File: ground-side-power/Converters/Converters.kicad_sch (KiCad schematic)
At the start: 31 parts, among them J10 Conn_01x03_Female, J12 Conn_01x04_Female, J13 DAQ Voltage Sensing, J14 DAQ Current Sensing, J27 Conn_01x02_Female, U3 K7805-3AR3, U4 INA180, U5 INA180, U6 URB2424LD-20WR3

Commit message: Resolved Final Issues
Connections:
- net +5V: now also J27.2 (Pin_2); no longer J27.1 (Pin_1)
- net +BATT: now also J10.2 (Pin_2); no longer J10.1 (Pin_1)
- net GND: now also J10.1 (Pin_1), J27.1 (Pin_1); no longer J10.2 (Pin_2), J27.2 (Pin_2)
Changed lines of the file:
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@@
     (effects (font (size 1.27 1.27)) (justify right))
   )
-  (hierarchical_label "+BATT" (shape input) (at 179.324 31.75 180)
+  (hierarchical_label "+BATT" (shape input) (at 179.324 34.29 180)
     (effects (font (size 1.27 1.27)) (justify right))
   )
-  (hierarchical_label "GND" (shape input) (at 179.197 54.991 180)
+  (hierarchical_label "GND" (shape input) (at 179.07 52.324 180)
     (effects (font (size 1.27 1.27)) (justify right))
   )
@@
     (effects (font (size 1.27 1.27)) (justify left))
   )
-  (hierarchical_label "+5V" (shape input) (at 179.197 52.451 180)
+  (hierarchical_label "+5V" (shape input) (at 179.07 54.864 180)
     (effects (font (size 1.27 1.27)) (justify right))
   )
@@
     (effects (font (size 1.27 1.27)) (justify right))
   )
-  (hierarchical_label "GND" (shape input) (at 179.324 34.29 180)
+  (hierarchical_label "GND" (shape input) (at 179.324 31.75 180)
     (effects (font (size 1.27 1.27)) (justify right))
   )
@@
     (pin "2")
   )
-  (symbol (lib_id "Connector:Conn_01x02_Female") (at 184.277 52.451 0) (unit 1)
-    (in_bom yes) (on_board yes) (fields_autoplaced)
-    (property "Reference" "J27" (id 0) (at 186.182 52.4509 0)
-      (effects (font (size 1.27 1.27)) (justify left))
-    )
-    (property "Value" "Conn_01x02_Female" (id 1) (at 186.182 54.9909 0)
-      (effects (font (size 1.27 1.27)) (justify left))
-    )
-    (property "Footprint" "GSP:1935310" (id 2) (at 184.277 52.451 0)
-      (effects (font (size 1.27 1.27)) hide)
-    )
-    (property "Datasheet" "~" (id 3) (at 184.277 52.451 0)
+  (symbol (lib_id "Connector:Conn_01x02_Female") (at 184.15 52.324 0) (unit 1)
+    (in_bom yes) (on_board yes) (fields_autoplaced)
+    (property "Reference" "J27" (id 0) (at 186.055 52.3239 0)
+      (effects (font (size 1.27 1.27)) (justify left))
+    )
+    (property "Value" "Conn_01x02_Female" (id 1) (at 186.055 54.8639 0)
+      (effects (font (size 1.27 1.27)) (justify left))
+    )
+    (property "Footprint" "GSP:1935310" (id 2) (at 184.15 52.324 0)
+      (effects (font (size 1.27 1.27)) hide)
+    )
+    (property "Datasheet" "~" (id 3) (at 184.15 52.324 0)
       (effects (font (size 1.27 1.27)) hide)
     )
@@
     )
     (path "/ed29890c-0b77-44d2-9f50-cf8ab77ebebf"
-      (reference "C10") (unit 1) (value "22uF") (footprint "Capacitor_SMD:C_0603_1608Metric_Pad1.08x0.95mm_HandSolder")
+      (reference "C10") (unit 1) (value "22uF") (footprint "Capacitor_SMD:C_0805_2012Metric_Pad1.18x1.45mm_HandSolder")
     )
     (path "/f316a14f-f1b7-4328-a910-be46f7f6ffff"
-      (reference "C11") (unit 1) (value "10uF") (footprint "Capacitor_SMD:C_0603_1608Metric_Pad1.08x0.95mm_HandSolder")
+      (reference "C11") (unit 1) (value "10uF") (footprint "Capacitor_SMD:C_0805_2012Metric_Pad1.18x1.45mm_HandSolder")
     )
     (path "/83e828f1-ea2c-4f92-a465-0be77eac1d2c"
-      (reference "C12") (unit 1) (value "10uF") (footprint "Capacitor_SMD:C_0603_1608Metric_Pad1.08x0.95mm_HandSolder")
+      (reference "C12") (unit 1) (value "10uF") (footprint "Capacitor_SMD:C_0805_2012Metric_Pad1.18x1.45mm_HandSolder")
     )
     (path "/578141ae-1aaf-4f14-b558-280a5eaf5853"
@@
     )
     (path "/9d81fb28-1d45-4a2d-a977-2809dd759a70"
-      (reference "C16") (unit 1) (value "10uF") (footprint "Capacitor_SMD:C_0603_1608Metric_Pad1.08x0.95mm_HandSolder")
+      (reference "C16") (unit 1) (value "10uF") (footprint "Capacitor_SMD:C_0805_2012Metric_Pad1.18x1.45mm_HandSolder")
     )
     (path "/6f03478f-34bb-4da3-ad2a-991c9dd3d62e"
@@
     )
     (path "/ec4fb15f-bcf3-43b3-a0ad-950a7d37eeb2"
-      (reference "R7") (unit 1) (value "0.01") (footprint "Resistor_SMD:R_1206_3216Metric_Pad1.30x1.75mm_HandSolder")
+      (reference "R7") (unit 1) (value "0.01") (footprint "Resistor_SMD:R_2512_6332Metric_Pad1.40x3.35mm_HandSolder")
     )
     (path "/e8b451aa-1d20-4320-9206-3705bb383e9f"
@@
     )
     (path "/1ccb64be-3251-49e5-9086-335694a2674c"
-      (reference "R9") (unit 1) (value "0.04") (footprint "Resistor_SMD:R_1206_3216Metric_Pad1.30x1.75mm_HandSolder")
+      (reference "R9") (unit 1) (value "0.04") (footprint "Resistor_SMD:R_2512_6332Metric_Pad1.40x3.35mm_HandSolder")
     )
     (path "/bb5b8186-e312-4770-869b-17d2c304a143"

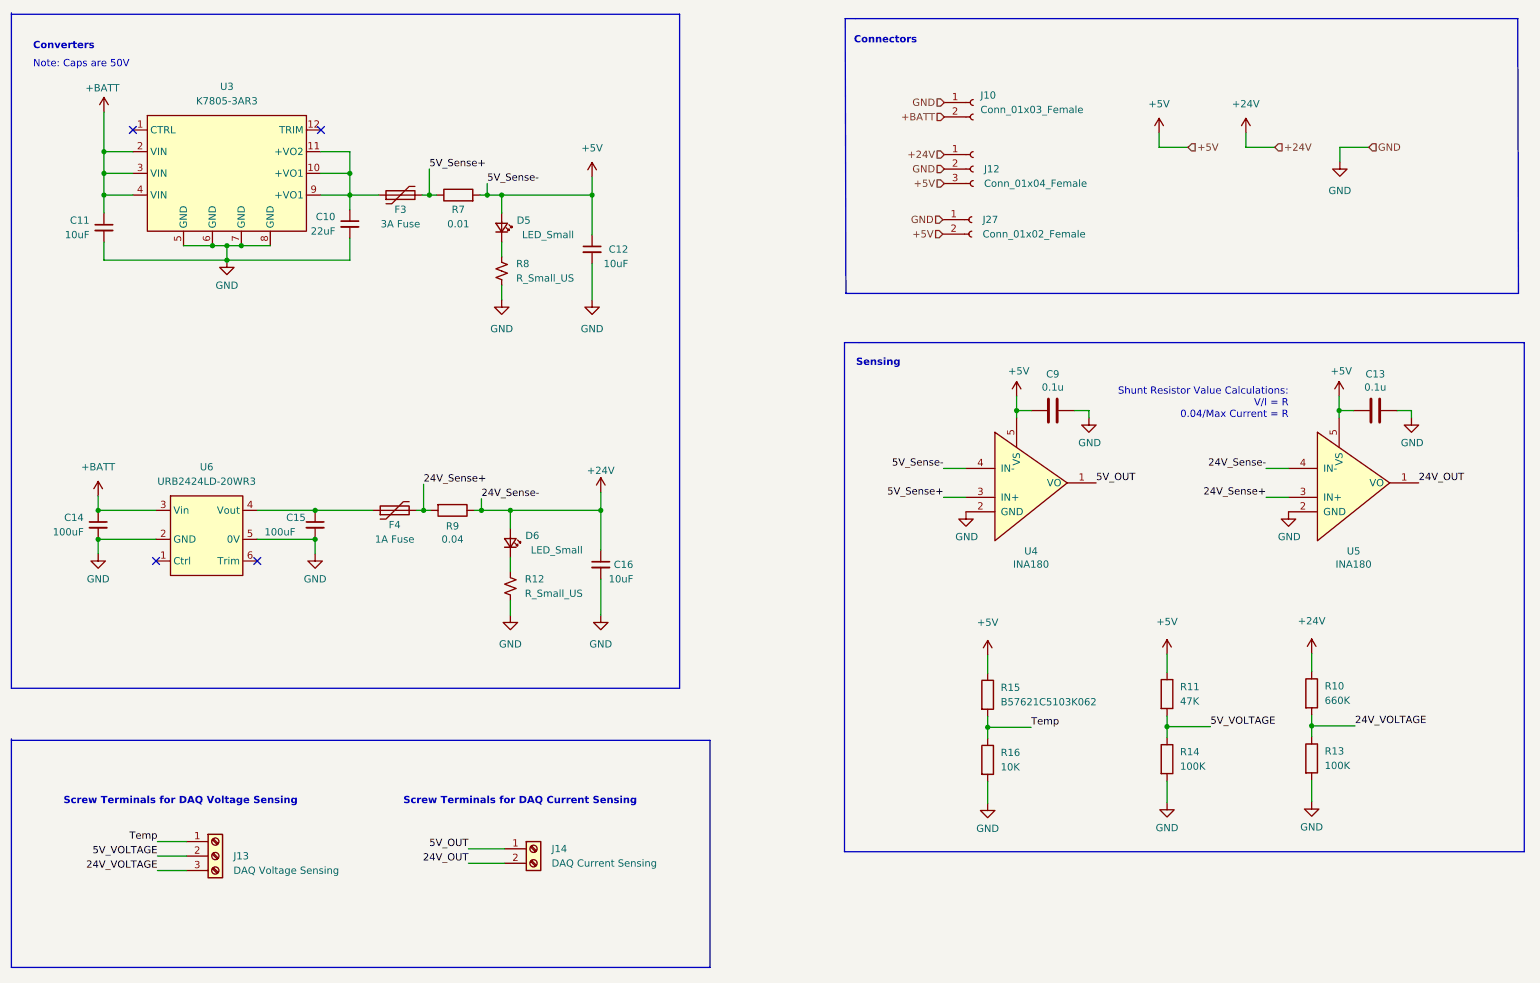
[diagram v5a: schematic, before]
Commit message: Fixed footprint issue
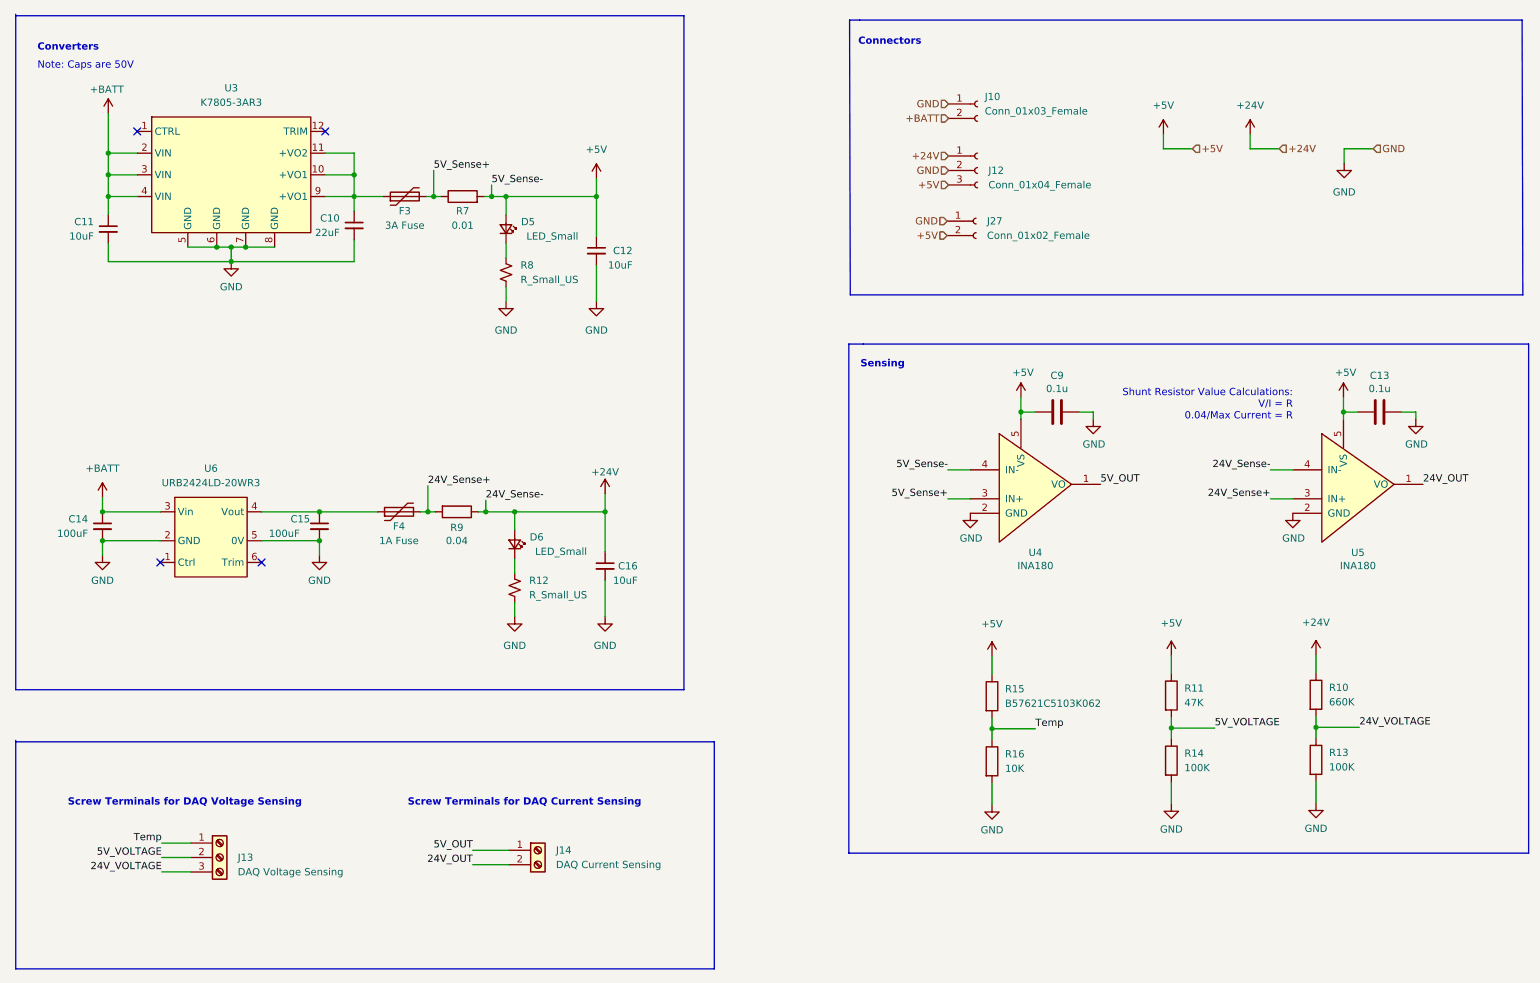
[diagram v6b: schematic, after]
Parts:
- C10, C11, C12, C16: footprint Capacitor_SMD:C_0603_1608Metric_Pad1.08x0.95mm_HandSolder -> Capacitor_SMD:C_0805_2012Metric_Pad1.18x1.45mm_HandSolder
- R7, R9: footprint Resistor_SMD:R_1206_3216Metric_Pad1.30x1.75mm_HandSolder -> Resistor_SMD:R_2512_6332Metric_Pad1.40x3.35mm_HandSolder
